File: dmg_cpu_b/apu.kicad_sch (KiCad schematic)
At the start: 0 parts

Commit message: Add legal stuff to title box
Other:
- company: (none) -> CC-BY-SA-4.0 Régis Galland & Michael Singer -- Derived work from Furrtek
- title: (none) -> DMG CPU B
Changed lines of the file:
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@@
 (kicad_sch (version 20211123) (generator eeschema)
   (paper "A4")
+  (title_block
+    (title "DMG CPU B")
+    (date "2022-02-01")
+    (rev "0")
+    (company "CC-BY-SA-4.0 Régis Galland & Michael Singer -- Derived work from Furrtek")
+    (comment 1 "https://github.com/msinger/dmg-schematics")
+  )
   (sheet (at 115.57 76.835) (size 52.07 25.4) (fields_autoplaced)
     (stroke (width 0.1524) (type solid) (color 0 0 0 0))

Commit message: Sheet 1 captured.
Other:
- removed sheet CLOCKS AND RESET
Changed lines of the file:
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@@
     (comment 1 "https://github.com/msinger/dmg-schematics")
   )
-  (sheet (at 115.57 76.835) (size 52.07 25.4) (fields_autoplaced)
-    (stroke (width 0.1524) (type solid) (color 0 0 0 0))
-    (fill (color 0 0 0 0.0000))
-    (property "Sheet name" "CLOCKS AND RESET" (id 0) (at 115.57 76.1234 0)
-      (effects (font (size 1.27 1.27)) (justify left bottom))
-    )
-    (property "Sheet file" "clocks_and_reset.kicad_sch" (id 1) (at 115.57 102.8196 0)
-      (effects (font (size 1.27 1.27)) (justify left top))
-    )
-  )
 )

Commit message: APU started: control regs, APU address decoding.
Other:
- added sheet APU DECODE (apu_decode.kicad_sch)
- added sheet CH1 REGS (ch1_regs.kicad_sch)
- added sheet FF24 FF25 CHAN ENABLE & VOLUME (ff24_ff25.kicad_sch)
- added sheet FF26 APU CLOCKS & RESETS (apu_control.kicad_sch)

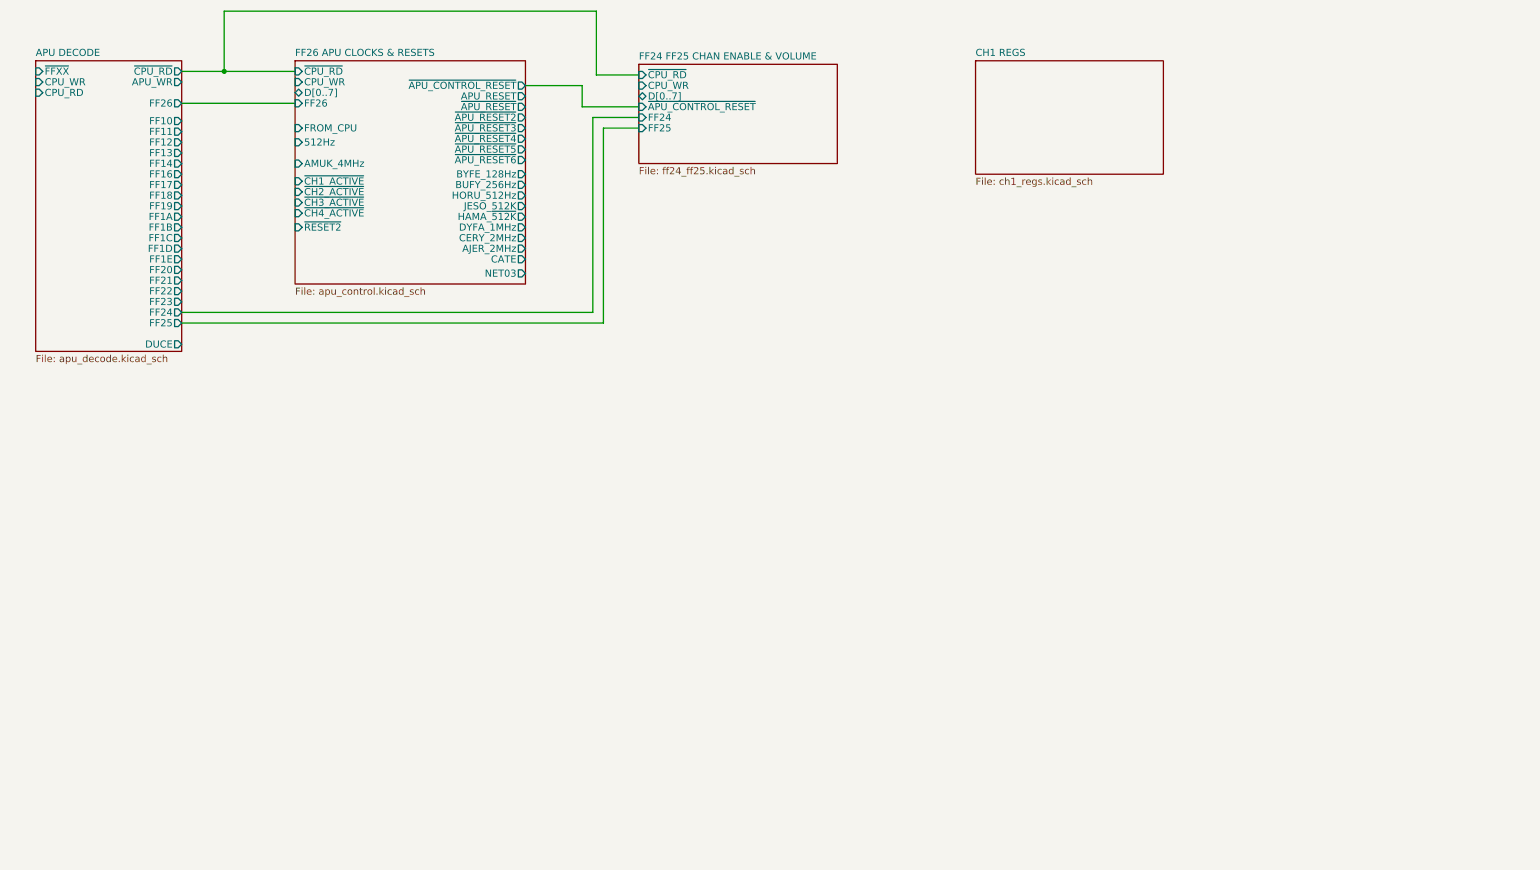
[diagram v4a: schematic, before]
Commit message: CH1 Regs page completed.
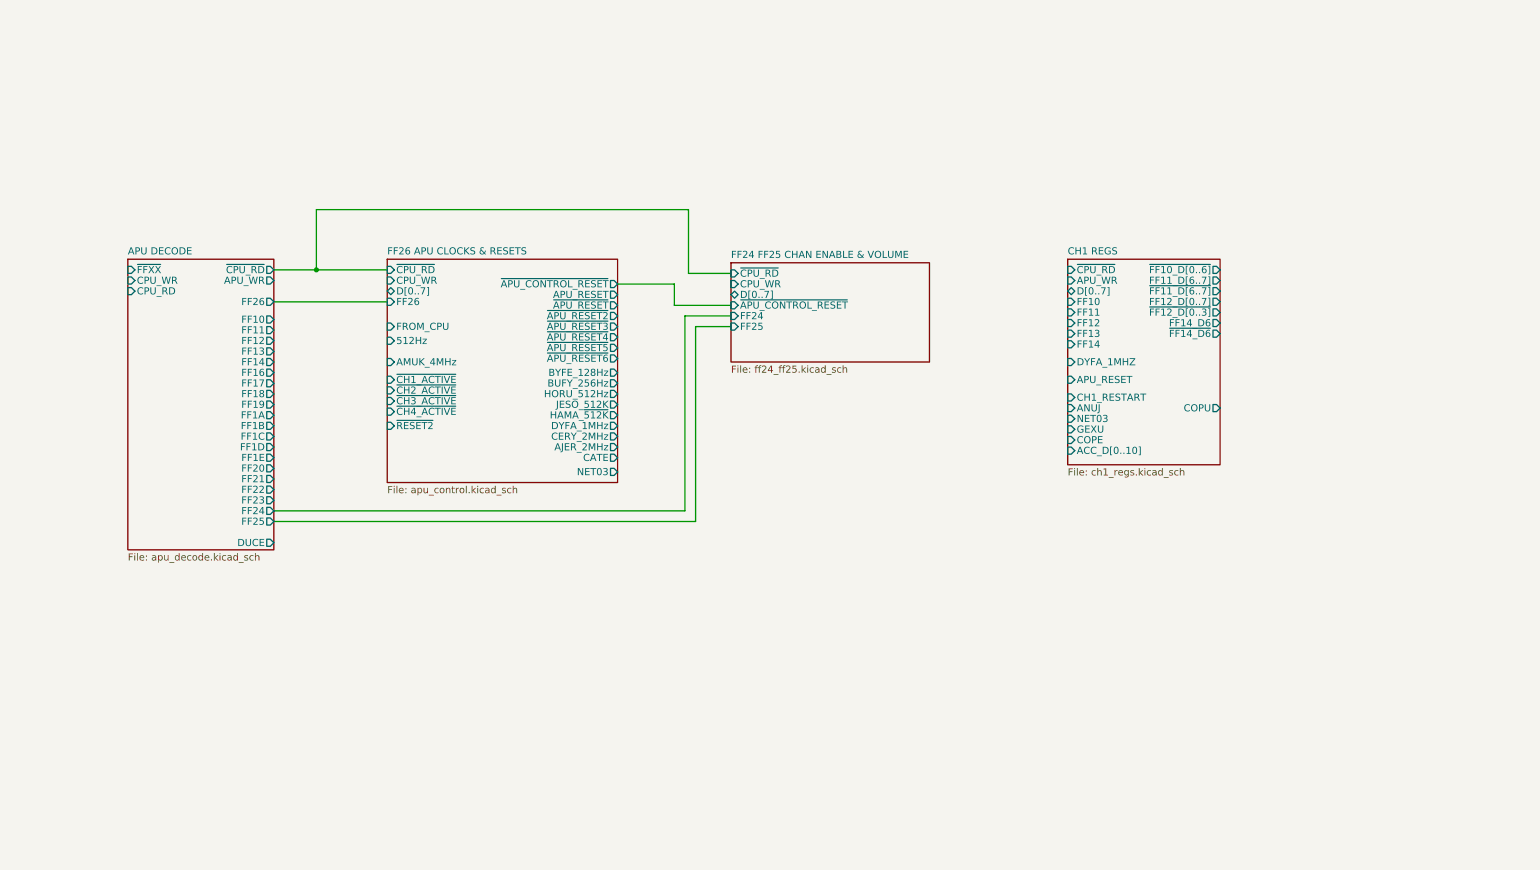
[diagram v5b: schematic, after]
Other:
- sheet CH1 REGS ports: added ACC_D[0..10], ANUJ, APU_RESET, APU_WR, CH1_RESTART, COPE, COPU, DYFA_1MHZ, D[0..7], FF10, FF11, FF11_D[6..7], FF12, FF12_D[0..7], FF13, FF14, FF14_D6, GEXU, NET03, ~{CPU_RD}, ~{FF10_D[0..6]}, ~{FF11_D[6..7]}, ~{FF12_D[0..3]}, ~{FF14_D6}; removed none

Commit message: CH2 Reg page added.
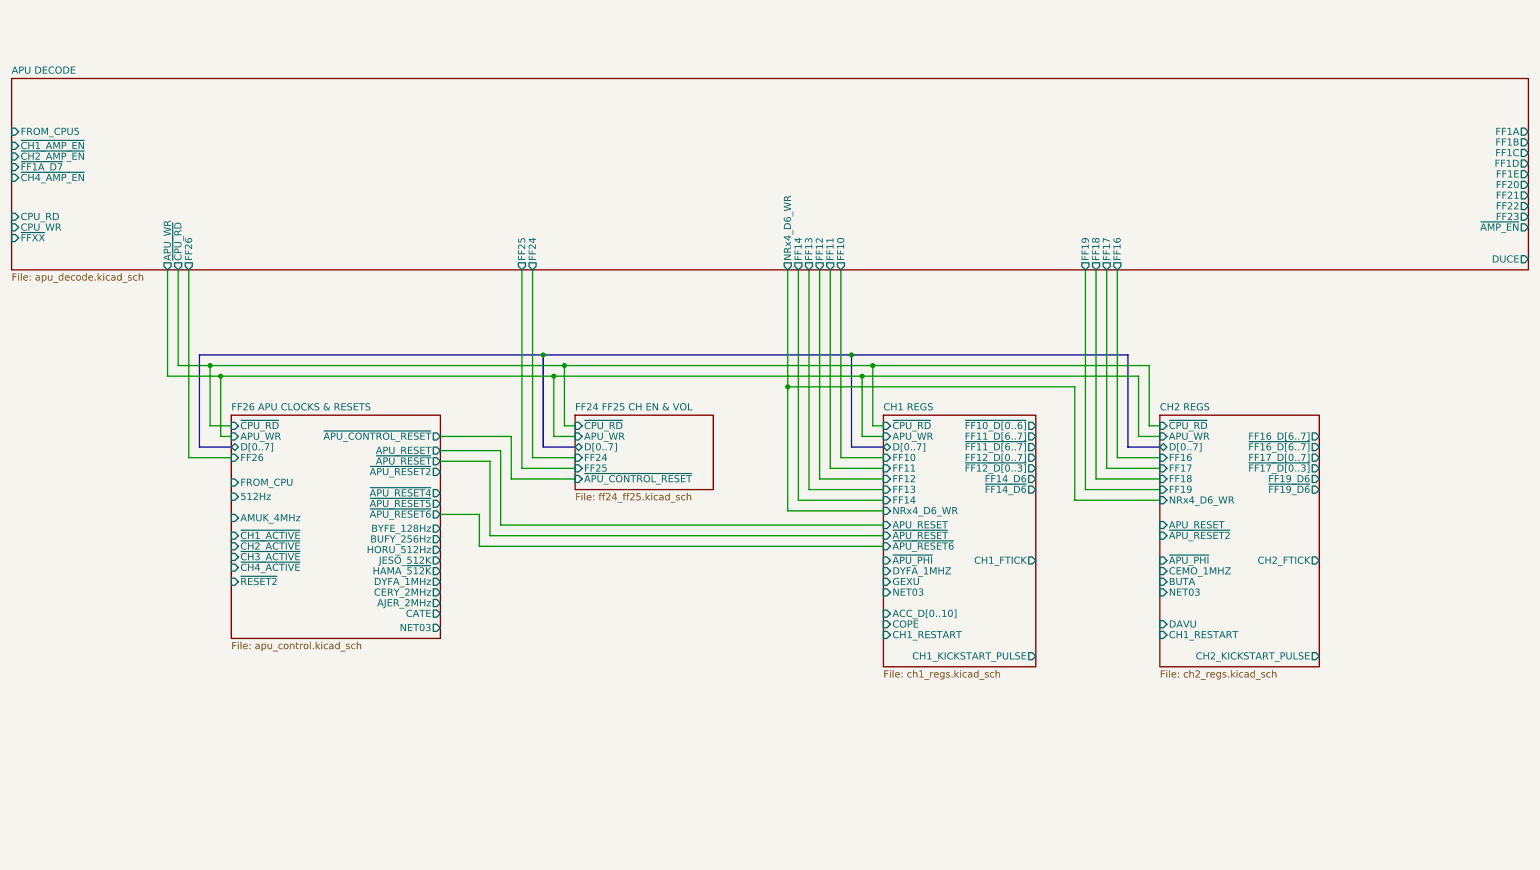
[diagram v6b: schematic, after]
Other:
- sheet FF24 FF25 CHAN ENABLE & VOLUME renamed FF24 FF25 CH EN & VOL
- added sheet CH2 REGS (ch2_regs.kicad_sch)
- sheet APU DECODE ports: added FROM_CPU5, NRx4_D6_WR, ~{AMP_EN}, ~{CH1_AMP_EN}, ~{CH2_AMP_EN}, ~{CH4_AMP_EN}, ~{FF1A_D7}; removed none
- sheet CH1 REGS ports: added CH1_FTICK, CH1_KICKSTART_PULSE, NRx4_D6_WR, ~{APU_PHI}, ~{APU_RESET6}, ~{APU_RESET}; removed ANUJ, COPU
- sheet FF24 FF25 CH EN & VOL ports: added APU_WR; removed CPU_WR
- sheet FF26 APU CLOCKS & RESETS ports: added APU_WR; removed CPU_WR, ~{APU_RESET3}

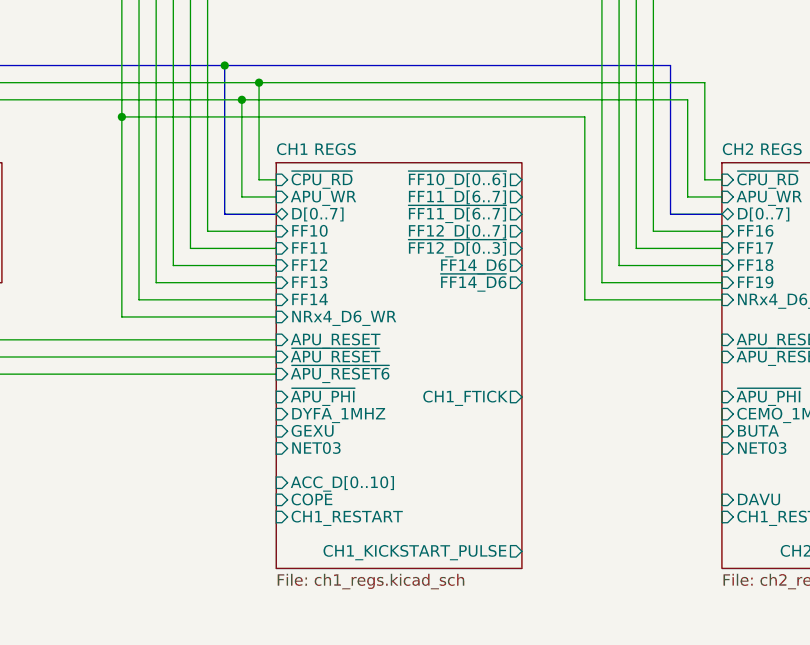
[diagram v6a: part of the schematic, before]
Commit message: Crammed more gates in CH1 REGS page to include all read and writes to FF13-14.
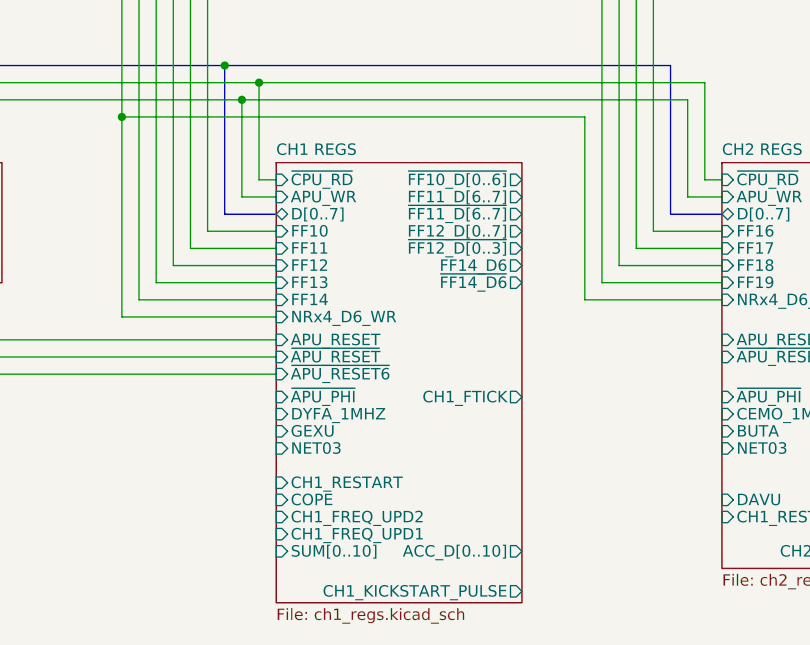
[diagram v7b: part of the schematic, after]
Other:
- sheet CH1 REGS ports: added CH1_FREQ_UPD1, CH1_FREQ_UPD2, SUM[0..10]; removed none
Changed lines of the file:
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@@
     )
   )
-  (sheet (at 195.58 98.425) (size 27.305 45.085) (fields_autoplaced)
+  (sheet (at 195.58 98.425) (size 27.305 48.895) (fields_autoplaced)
     (stroke (width 0.1524) (type solid) (color 0 0 0 0))
     (fill (color 0 0 0 0.0000))
@@
       (effects (font (size 1.27 1.27)) (justify left bottom))
     )
-    (property "Sheet file" "ch1_regs.kicad_sch" (id 1) (at 195.58 144.0946 0)
+    (property "Sheet file" "ch1_regs.kicad_sch" (id 1) (at 195.58 147.9046 0)
       (effects (font (size 1.27 1.27)) (justify left top))
     )
@@
       (effects (font (size 1.27 1.27)) (justify left))
     )
-    (pin "CH1_RESTART" input (at 195.58 137.795 180)
+    (pin "CH1_RESTART" input (at 195.58 133.985 180)
       (effects (font (size 1.27 1.27)) (justify left))
     )
@@
     )
     (pin "FF13" input (at 195.58 111.76 180)
-      (effects (font (size 1.27 1.27)) (justify left))
-    )
-    (pin "ACC_D[0..10]" input (at 195.58 133.985 180)
       (effects (font (size 1.27 1.27)) (justify left))
     )
@@
       (effects (font (size 1.27 1.27)) (justify left))
     )
-    (pin "CH1_KICKSTART_PULSE" output (at 222.885 141.605 0)
+    (pin "CH1_KICKSTART_PULSE" output (at 222.885 146.05 0)
       (effects (font (size 1.27 1.27)) (justify right))
     )
@@
       (effects (font (size 1.27 1.27)) (justify right))
     )
+    (pin "CH1_FREQ_UPD1" input (at 195.58 139.7 180)
+      (effects (font (size 1.27 1.27)) (justify left))
+    )
+    (pin "CH1_FREQ_UPD2" input (at 195.58 137.795 180)
+      (effects (font (size 1.27 1.27)) (justify left))
+    )
+    (pin "SUM[0..10]" input (at 195.58 141.605 180)
+      (effects (font (size 1.27 1.27)) (justify left))
+    )
+    (pin "ACC_D[0..10]" output (at 222.885 141.605 0)
+      (effects (font (size 1.27 1.27)) (justify right))
+    )

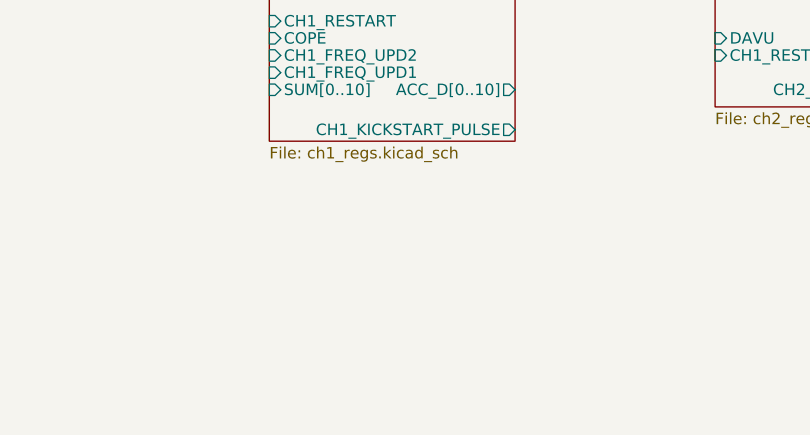
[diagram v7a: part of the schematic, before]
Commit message: CH1 SWEEP page added.
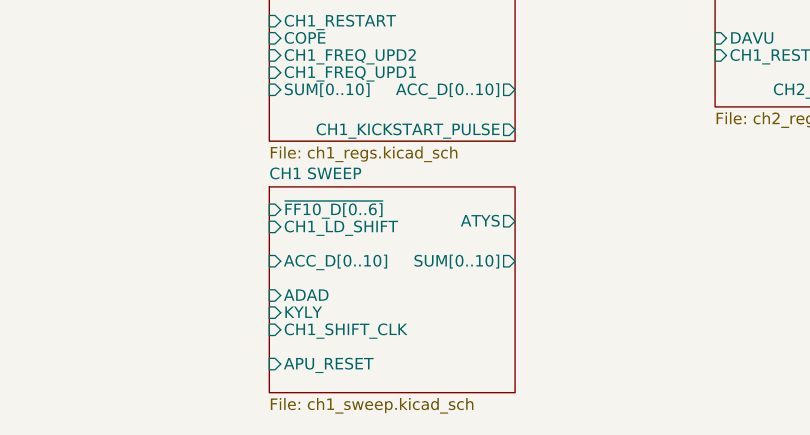
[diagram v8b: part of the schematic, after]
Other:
- added sheet CH1 SWEEP (ch1_sweep.kicad_sch)
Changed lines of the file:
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@@
+    )
+  )
+  (sheet (at 195.58 152.4) (size 27.305 22.86) (fields_autoplaced)
+    (stroke (width 0.1524) (type solid) (color 0 0 0 0))
+    (fill (color 0 0 0 0.0000))
+    (property "Sheet name" "CH1 SWEEP" (id 0) (at 195.58 151.6884 0)
+      (effects (font (size 1.27 1.27)) (justify left bottom))
+    )
+    (property "Sheet file" "ch1_sweep.kicad_sch" (id 1) (at 195.58 175.8446 0)
+      (effects (font (size 1.27 1.27)) (justify left top))
+    )
+    (pin "SUM[0..10]" output (at 222.885 160.655 0)
+      (effects (font (size 1.27 1.27)) (justify right))
+    )
+    (pin "CH1_LD_SHIFT" input (at 195.58 156.845 180)
+      (effects (font (size 1.27 1.27)) (justify left))
+    )
+    (pin "APU_RESET" input (at 195.58 172.085 180)
+      (effects (font (size 1.27 1.27)) (justify left))
+    )
+    (pin "ACC_D[0..10]" input (at 195.58 160.655 180)
+      (effects (font (size 1.27 1.27)) (justify left))
+    )
+    (pin "CH1_SHIFT_CLK" input (at 195.58 168.275 180)
+      (effects (font (size 1.27 1.27)) (justify left))
+    )
+    (pin "ATYS" output (at 222.885 156.21 0)
+      (effects (font (size 1.27 1.27)) (justify right))
+    )
+    (pin "ADAD" input (at 195.58 164.465 180)
+      (effects (font (size 1.27 1.27)) (justify left))
+    )
+    (pin "KYLY" input (at 195.58 166.37 180)
+      (effects (font (size 1.27 1.27)) (justify left))
+    )
+    (pin "~{FF10_D[0..6]}" input (at 195.58 154.94 180)
+      (effects (font (size 1.27 1.27)) (justify left))
     )
   )
